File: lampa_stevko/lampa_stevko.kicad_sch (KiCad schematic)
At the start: 86 parts, among them J1 Conn_01x04_Pin, P1 USB_C_Plug_USB2.0, Q1 AO3400A, SW1 B3U-1000P, SW2 B3U-1000P, SW3 B3U-1000P, U1 STM32U073KCUx, U2 IP4234CZ6, U3 MCP6L01x-xOT, U4 STNS01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

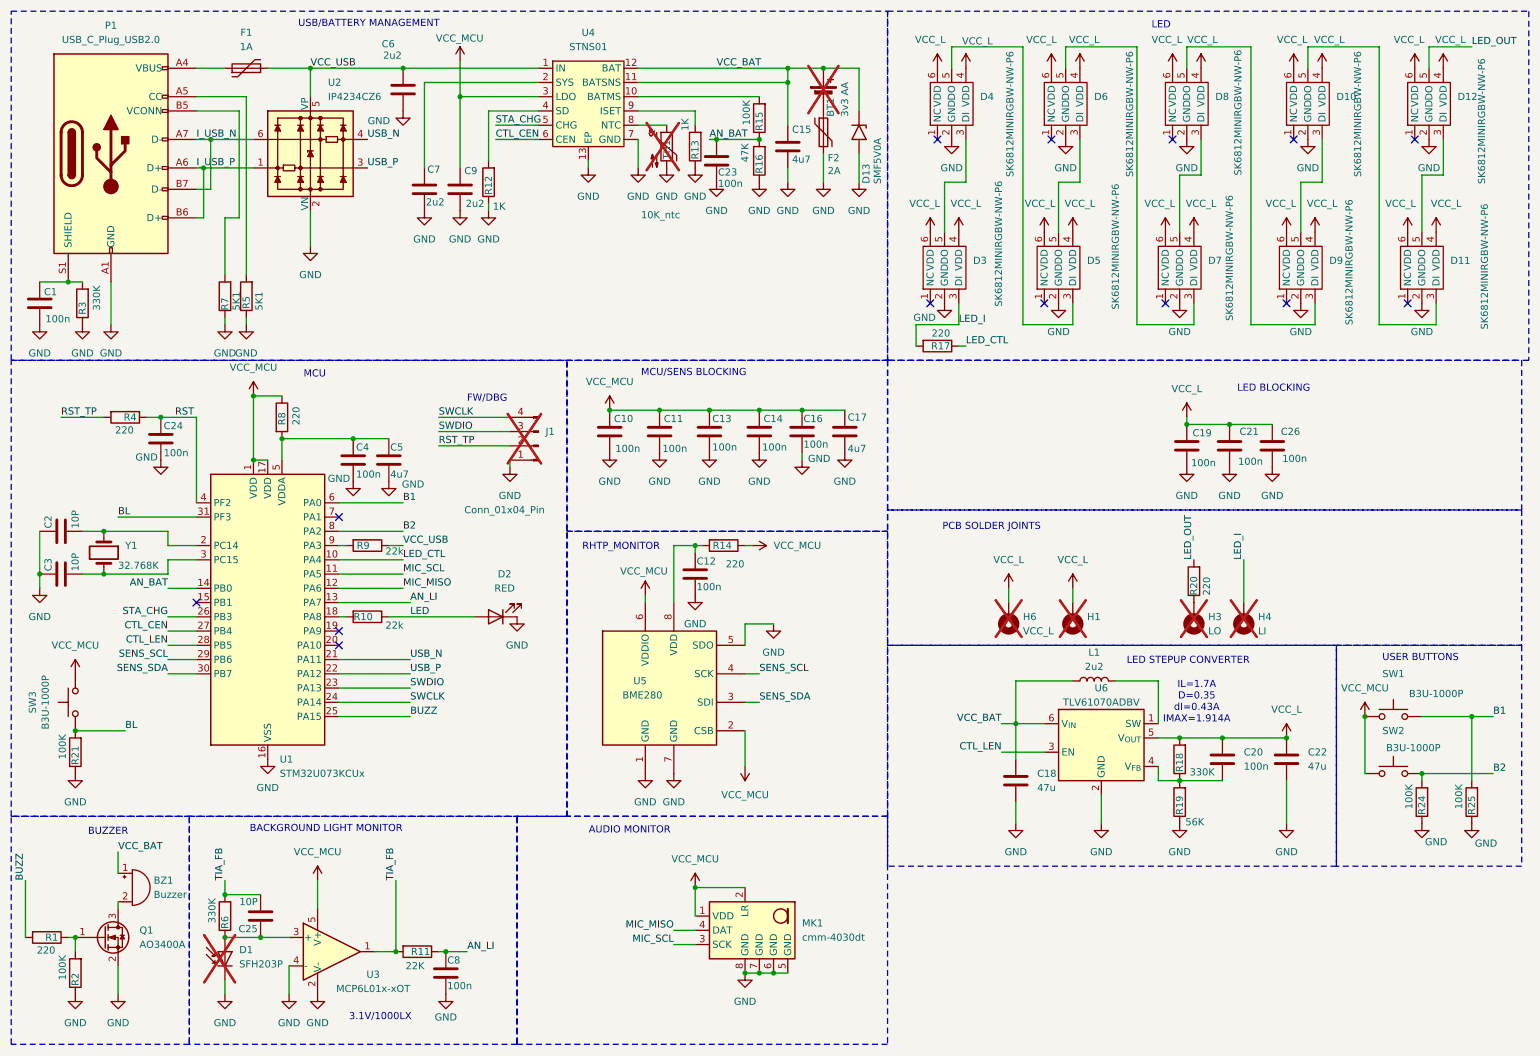
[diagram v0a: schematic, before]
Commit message: prepinanie pamati-b1nastavit dlhsie ako 2s mic debbug pouzity no mic nejde bootloader neopraveny inak to vyzera dobre
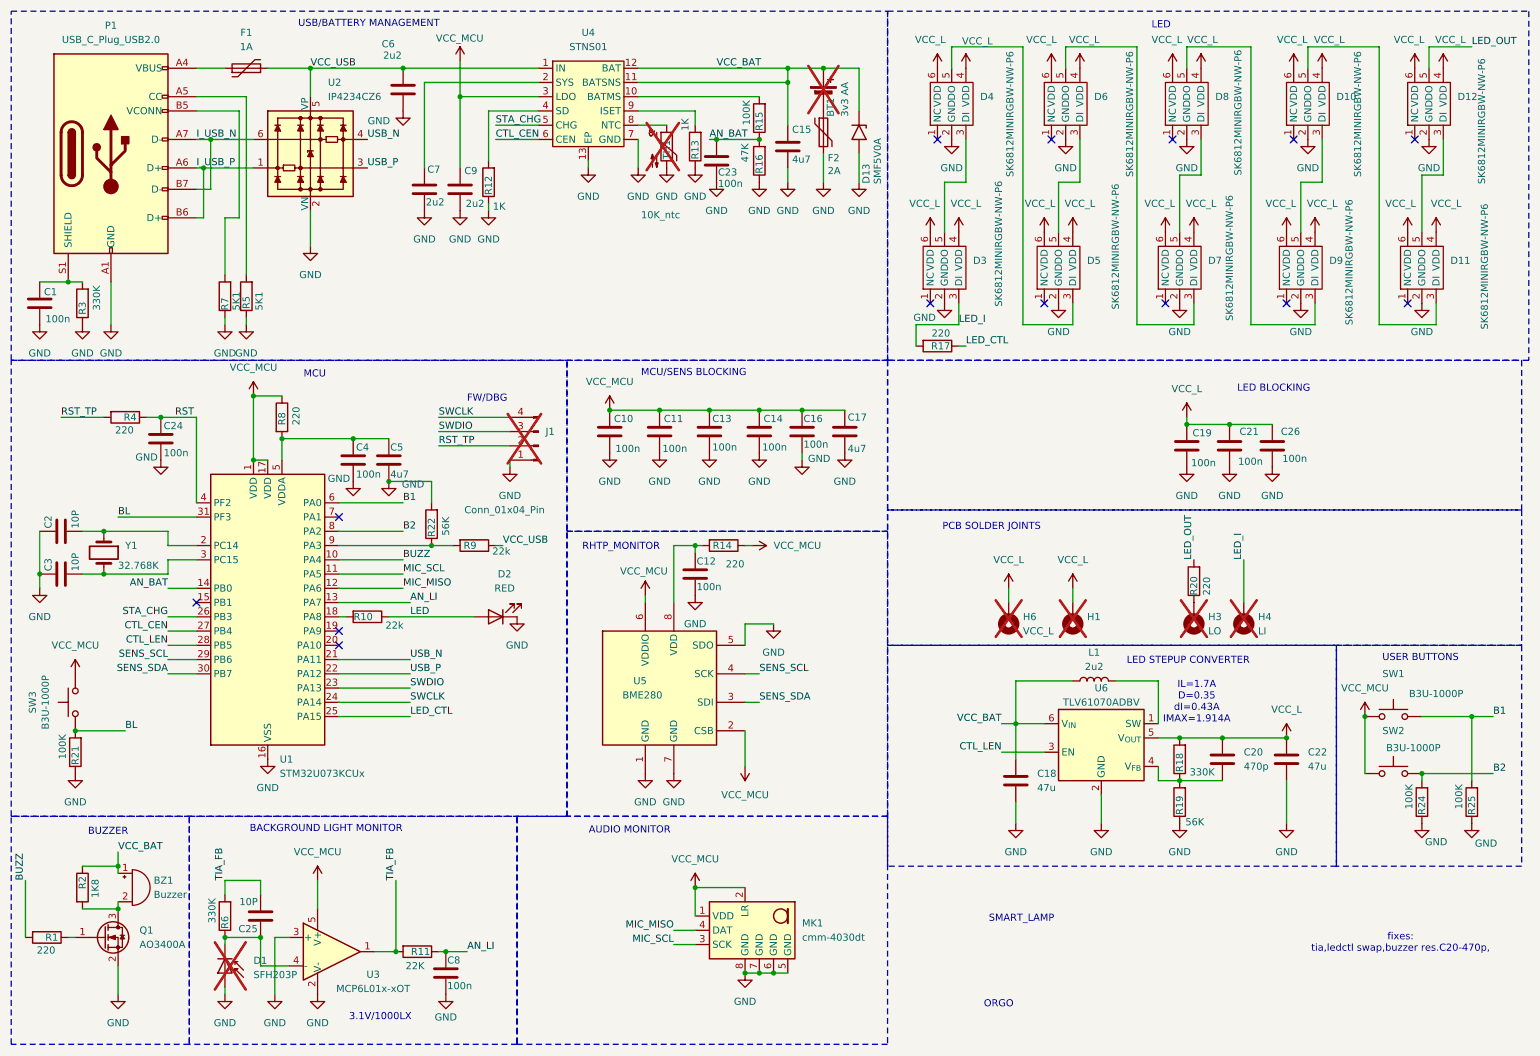
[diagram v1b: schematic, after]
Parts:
- added R22: 56K, Resistor_SMD:R_0603_1608Metric, symbol Device:R
- C20: value 100n -> 470p; LCSC C66501 -> (none); MPN CL10B104KO8NNNC -> (none); PRICE 0.006 -> (none)
- R2: value 100K -> 1K8; LCSC C14675 -> C107696; MPN RC0603FR-07100KL -> RC0603FR-07220RL
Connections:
- net BUZZ: now also U1.10 (PA4); no longer U1.25 (PA15)
- net GND: now also D1.2 (A), U3.3 (+), R22.2; no longer D1.1 (K), R2.1, U3.4 (-)
- net LED_CTL: now also U1.25 (PA15); no longer U1.10 (PA4)
- net VCC_BAT: now also R2.1
- net at C25.1, R6.1: now also D1.1 (K), U3.4 (-); no longer D1.2 (A), U3.3 (+)
- net at Q1.1 (G), R1.1: no longer R2.2
- net at BZ1.2 (-), Q1.3 (D): now also R2.2
- net at R9.2, U1.9 (PA3): now also R22.1
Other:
- note added: "ORGO"
- note added: "SMART_LAMP"
- note added: "fixes: tia,ledctl swap,buzzer res.C20-470p,"
- moved on the sheet: D1, R9
